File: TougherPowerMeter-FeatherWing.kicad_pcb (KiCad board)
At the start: 2 copper layers, 64 parts, among them J1 Jumper, J10 796639-2, J11 Jumper, J2 796639-2, J3 796639-2, J4 796639-2, J5 796639-2, J6 796639-2, J7 796639-2, J8 796639-2, J9 796639-2, U1 AP63205, U2 TPS1HB08A-Q1, U3 FeatherWing, U4 INA3221

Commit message: Finish design
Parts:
- added A1: Arduino_Nano_v3.x, Module_BD:Arduino_Nano_NoSilk, F.Cu at (195.4, 59.7)
- added C18: 4.7uF, Capacitor_SMD:C_0603_1608Metric, B.Cu at (156.7, 57.8)
- added C19: 100n, Resistor_SMD:R_0603_1608Metric, B.Cu at (217.7, 83.1)
- added C20: 220n, Capacitor_SMD:C_0603_1608Metric, B.Cu at (120.3, 75.5)
- added C21: 22u, Capacitor_SMD:C_1210_3225Metric, B.Cu at (191.4, 99.5)
- added C22: 10u, Capacitor_SMD:C_1206_3216Metric, B.Cu at (199.9, 92.7)
- added C23: 22u, Capacitor_SMD:C_0805_2012Metric, B.Cu at (204.5, 90.2)
- added D8: D_Schottky, Diode_SMD:D_SMB, B.Cu at (189.2, 93.1)
- added F1: 0ZCG0075BF2B, Fuse:Fuse_1812_4532Metric, B.Cu at (203.7, 83.8)
- added H1: MountingHole, MountingHole:MountingHole_3.2mm_M3_Pad_Via, F.Cu at (97.8, 56.2)
- added H2: MountingHole, MountingHole:MountingHole_3.2mm_M3_Pad_Via, F.Cu at (219.8, 56.2)
- added H3: MountingHole, MountingHole:MountingHole_3.2mm_M3_Pad_Via, F.Cu at (97.8, 101.2)
- added H4: MountingHole, MountingHole:MountingHole_3.2mm_M3_Pad_Via, F.Cu at (219.8, 101.2)
- added R25: 10k, Resistor_SMD:R_0603_1608Metric, B.Cu at (125.3, 64.7)
- added R26: 10k, Resistor_SMD:R_0603_1608Metric, B.Cu at (125.3, 66.6)
- C1: value 10u -> 4.7uF; footprint Capacitor_SMD:C_1206_3216Metric -> Capacitor_SMD:C_0603_1608Metric; moved to B.Cu
- C10, C11, C12, C13, C14, C15, C16, C17, C4, C5, C8, C9, D1, D2, D3, D4, D5, D6, D7, L1, R1, R10, R11, R12, R13, R14, R15, R16, R17, R18, R19, R20, R21, R22, R23, R24, R5, R6, R7, R8, R9, U1, U2, U4: moved to B.Cu
- C2: value 220n -> 22u; footprint Capacitor_SMD:C_0603_1608Metric -> Capacitor_SMD:C_1210_3225Metric; moved to B.Cu
- C3: value 100n -> 10u; footprint Resistor_SMD:R_0603_1608Metric -> Capacitor_SMD:C_1206_3216Metric; moved to B.Cu
- C6: value 220n -> 22u; footprint Capacitor_SMD:C_0603_1608Metric -> Capacitor_SMD:C_0805_2012Metric; moved to B.Cu
- C7: value 22u -> 220n; footprint Capacitor_SMD:C_0805_2012Metric -> Capacitor_SMD:C_0603_1608Metric; moved to B.Cu
- R2: value 12k -> 220; moved to B.Cu
- R3: value 10k -> 220; moved to B.Cu
- R4: value 10k -> 12k; moved to B.Cu
- U3: footprint Module_BD:FeatherWing -> Module_BD:FeatherWing_NoMH
- moved U3 141.8 mm to (203.1, 78.8), turned to 180 degrees
- moved J1 130.9 mm to (180.6, 80.0), turned to 180 degrees
- moved J11 118.0 mm to (153.8, 76.2)
- moved U1 111.1 mm to (199.8, 98.4)
- moved R21 104.1 mm to (140.2, 79.8), turned to 180 degrees
- moved C1 95.0 mm to (207.5, 85.4), turned to 90 degrees
- moved R23 95.0 mm to (174.5, 78.8), turned to 270 degrees
- moved L1 90.4 mm to (205.6, 98.4)
- moved R22 90.3 mm to (170.0, 77.7), turned to 180 degrees
- moved R3 89.0 mm to (217.7, 87.1)
- moved C5 88.2 mm to (204.5, 92.2)
- moved R24 88.1 mm to (170.0, 79.8), turned to 180 degrees
- moved R5 88.1 mm to (217.7, 85.1)
- moved J10 86.0 mm to (108.4, 97.8)
- moved D7 86.0 mm to (165.6, 83.8), turned to 180 degrees
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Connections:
- net /current-sense-frontend-CH1/IS+ renamed /IN1_P
- net /current-sense-frontend-CH1/IS- renamed /IN1_N
- net /current-sense-frontend-CH2/IS+ renamed /IN2_P
- net /current-sense-frontend-CH2/IS- renamed /IN2_N
- net /current-sense-frontend-CH3/IS+ renamed /IN3_P
- net /current-sense-frontend-CH3/IS- renamed /IN3_N
- C1 pad 1: GND -> +3V3
- C1 pad 2: /CH1_OUT -> GND
- C2 pad 1: /CH3_IN -> GND
- C2 pad 2: GND -> Net-(C2-Pad2)
- C3 pad 1: /CH3_SNS -> GND
- C3 pad 2: GND -> Net-(C2-Pad2)
- C5 pad 2: +5V -> Net-(C23-Pad2)
- C6 pad 1: /current-sense-frontend-CH3/PIN -> GND
- C6 pad 2: GND -> Net-(C23-Pad2)
- C7 pad 1: GND -> /CH3_IN
- C7 pad 2: +5V -> GND
- J1 pad 1: Net-(J1-Pad1) -> /CH1_OUT
- J1 pad 2: +5V -> /buck/VIN
- J10 pad 1: GND -> /CH3_OUT
- J10 pad 2: /CH3_OUT -> GND
- J2 pad 1: GND -> /CH1_IN
- J2 pad 2: /CH1_IN -> GND
- J3 pad 1: GND -> /CH2_IN
- J3 pad 2: /CH2_IN -> GND
- J4 pad 1: GND -> /CH3_IN
- J4 pad 2: /CH3_IN -> GND
- J5 pad 1: GND -> /CH1_OUT
- J5 pad 2: /CH1_OUT -> GND
- J6 pad 1: GND -> /CH2_OUT
- J6 pad 2: /CH2_OUT -> GND
- J7 pad 1: GND -> /CH3_OUT
- J7 pad 2: /CH3_OUT -> GND
- J8 pad 1: GND -> /CH1_OUT
- J8 pad 2: /CH1_OUT -> GND
- J9 pad 1: GND -> /CH2_OUT
- J9 pad 2: /CH2_OUT -> GND
- L1 pad 2: +5V -> Net-(C23-Pad2)
- R1 pad 1: GND -> /SDA
- R10 pad 2: /SCL -> Net-(R10-Pad2)
- R2 pad 1: Net-(R2-Pad1) -> /SCL
- R2 pad 2: /CH3_IN -> Net-(R10-Pad2)
- R3 pad 1: /CH3_SNS -> GND
- R3 pad 2: Net-(R1-Pad2) -> Net-(R3-Pad2)
- R4 pad 2: /CH3_DIA_EN -> /CH3_IN
- R5 pad 1: Net-(R5-Pad1) -> /CH3_SNS
- R5 pad 2: /CH3_SEL -> Net-(R3-Pad2)
- R6 pad 2: /CH3_LATCH -> /CH3_DIA_EN
- R7 pad 2: /CH3_EN -> /CH3_SEL
- R8 pad 1: Net-(R8-Pad1) -> +3V3
- R9 pad 2: /SDA -> Net-(R1-Pad2)
- U1 pad 1: +5V -> Net-(C23-Pad2)
- U1 pad 2: /CH1_OUT -> Net-(C2-Pad2)
- U1 pad 3: /CH1_OUT -> Net-(C2-Pad2)
- U2 pad 14: Net-(R5-Pad1) -> Net-(R7-Pad1)
- U2 pad 16: Net-(R4-Pad1) -> Net-(R6-Pad1)
- U2 pad 2: Net-(R1-Pad2) -> Net-(R3-Pad2)
- U2 pad 3: Net-(R6-Pad1) -> Net-(R25-Pad1)
- U2 pad 4: Net-(R7-Pad1) -> Net-(R26-Pad1)
- U2 pad 5: Net-(R2-Pad1) -> Net-(R4-Pad1)
- U3 pad 26: Net-(J1-Pad1) -> +5V
- U4 pad 16: Net-(R8-Pad1) -> +3V3
- U4 pad 6: /SCL -> Net-(R10-Pad2)
- U4 pad 7: /SDA -> Net-(R1-Pad2)
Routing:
- net +3V3: track 0.00 -> 160.2 mm, vias 0 -> 9
- net /CH3_DIA_EN: track 0.00 -> 140.7 mm, vias 0 -> 2
- net Net-(R3-Pad2): track 0.00 -> 138.5 mm, vias 0 -> 2
- net /CH3_SEL: track 0.00 -> 102.2 mm, vias 0 -> 4
- net /IN3_N: track 0.00 -> 98.3 mm, vias 0 -> 2
- net /IN3_P: track 0.00 -> 96.4 mm
- net /CH3_EN: track 0.00 -> 90.7 mm, vias 0 -> 2
- net /CH3_LATCH: track 0.00 -> 87.6 mm, vias 0 -> 2
- net /IN2_N: track 0.00 -> 75.8 mm, vias 0 -> 2
- net /IN2_P: track 0.00 -> 73.1 mm
- net /TIMING_CTRL: track 0.00 -> 64.9 mm, vias 0 -> 3
- net /POWER_VALID: track 0.00 -> 63.6 mm
- net /WARNING: track 0.00 -> 62.1 mm
- net /CRITICAL: track 0.00 -> 61.6 mm
- net /SCL: track 0.00 -> 52.3 mm, vias 0 -> 2
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- added copper zone on B.Cu, net +5V
- added copper zone on B.Cu, net /CH1_IN
- added copper zone on B.Cu, net /CH1_OUT
- added copper zone on B.Cu, net /CH2_IN
- added copper zone on B.Cu, net /CH2_OUT
- added copper zone on B.Cu, net /CH3_IN
- added copper zone on B.Cu, net /CH3_OUT
- added copper zone on B.Cu, net /IN1_N
- added copper zone on B.Cu, net /IN1_P
- added copper zone on B.Cu, net /IN2_N
- added copper zone on B.Cu, net /IN2_P
- added copper zone on B.Cu, net /IN3_N
- added copper zone on B.Cu, net /IN3_P
- added copper zone on B.Cu, net /current-sense-frontend-CH3/PIN
- added copper zone on B.Cu, net GND
- added copper zone on F.Cu, net GND
- added copper zone on B.Cu, net Net-(C2-Pad2)
- added copper zone on B.Cu, net Net-(C23-Pad2)
- added copper zone on B.Cu, net Net-(C4-Pad1)
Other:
- board outline added: 130 x 53 mm
- net class Default: via_dia 0.8 -> 0.6; via_drill 0.4 -> 0.3
- net class INA3221_DIFF added: clearance 0.2, trace_width 0.2, via_dia 0.6, via_drill 0.3
- board text added: "+3.3V"
- board text added: "+5V"
- board text added: "1000000"
- board text added: "1000001"
- board text added: "500mA max"
- board text added: "Arduino Nano"
- board text added: "CH1"
- board text added: "CH2"
- board text added: "CH3"
- board text added: "CRIT"
- board text added: "DIAEN"
- board text added: "EN"
- board text added: "Feather"
- board text added: "GND"
- board text added: "I2C ADDR"
- board text added: "I2C PULLUP"
- board text added: "INPUT"
- board text added: "LATCH"
- board text added: "OUTPUT"
- board text added: "PM-MON-01 REV1.0-2020"
- board text added: "PWOK"
- board text added: "SCL"
- board text added: "SDA"
- board text added: "SEL"
- board text added: "SNS"
- board text added: "TCTL"
- board text added: "Tougher INA3221 Power Monitor beastdevices.com"
- board text added: "WARN"

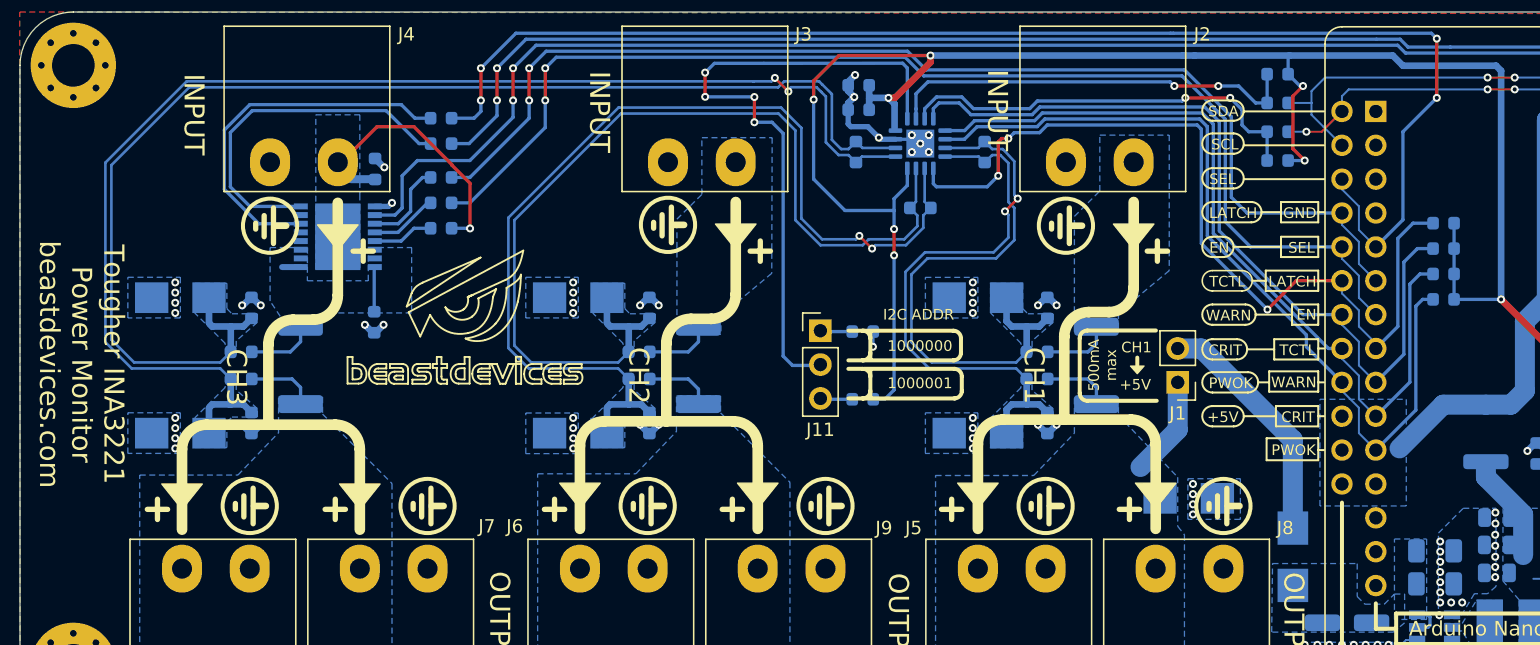
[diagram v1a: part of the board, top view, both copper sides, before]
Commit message: Add fiducials, fix aesthetics in schematics
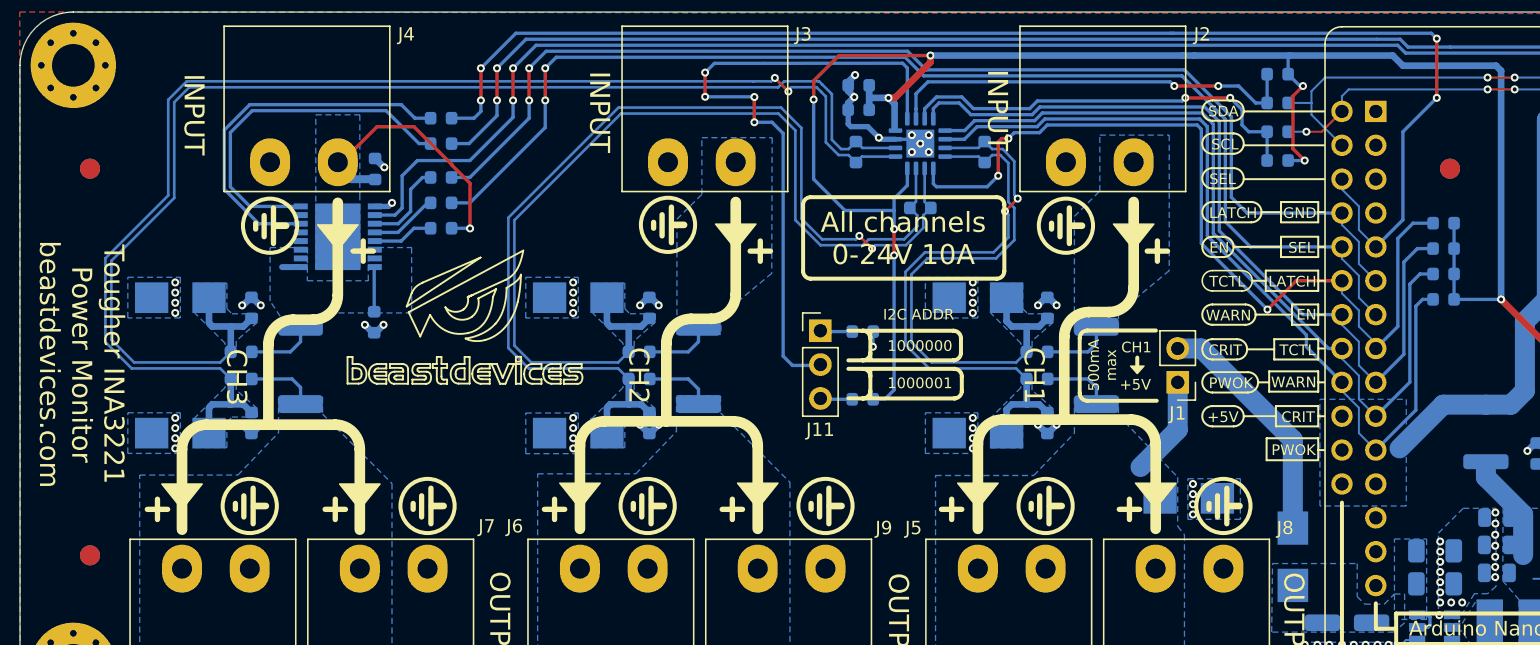
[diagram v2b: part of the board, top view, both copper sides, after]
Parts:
- added FID1: Fiducial, Fiducial:Fiducial_1.5mm_Mask4.5mm, F.Cu at (99.0, 93.0)
- added FID2: Fiducial, Fiducial:Fiducial_1.5mm_Mask4.5mm, F.Cu at (99.0, 64.0)
- added FID3: Fiducial, Fiducial:Fiducial_1.5mm_Mask4.5mm, F.Cu at (201.0, 64.0)
- added FID4: Fiducial, Fiducial:Fiducial_1.5mm_Mask4.5mm, B.Cu at (99.0, 64.0)
- added FID5: Fiducial, Fiducial:Fiducial_1.5mm_Mask4.5mm, B.Cu at (99.0, 93.0)
- added FID6: Fiducial, Fiducial:Fiducial_1.5mm_Mask4.5mm, B.Cu at (201.0, 64.0)
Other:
- board text added: "All channels 0-24V 10A"

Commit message: Add 3D renderings and update exported schematics
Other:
- rule trace_min: 0.2 -> 0.15
- rule via_min_size: 0.4 -> 0.3
